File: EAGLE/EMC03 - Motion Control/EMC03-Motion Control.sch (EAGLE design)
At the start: 206 parts, among them J1 UART0, J10 67997-108HLF, J11 67997-108HLF, J12 67997-108HLF, J13 67997-108HLF, J14 67997-108HLF, J15 67997-108HLF, J2 SWD, J3 USB-B, J4 MicroSD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

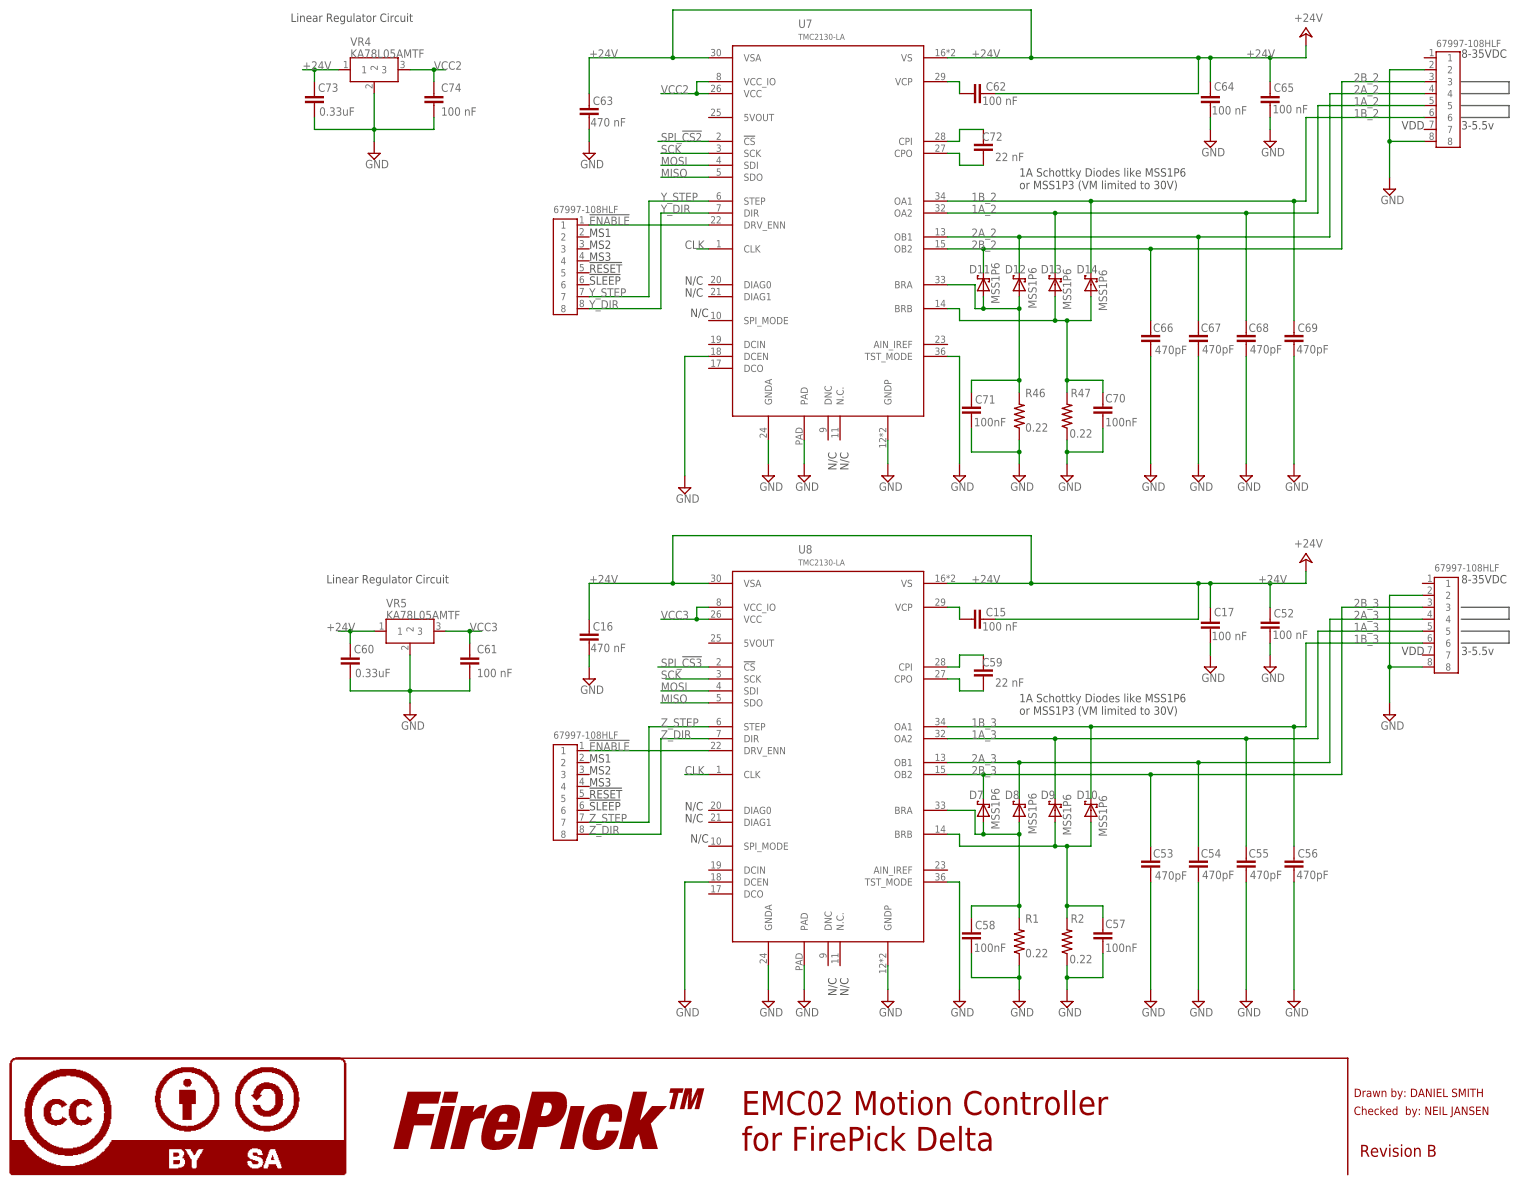
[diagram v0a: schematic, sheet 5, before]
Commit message: Updated BOM, Database, Schematic for final parts
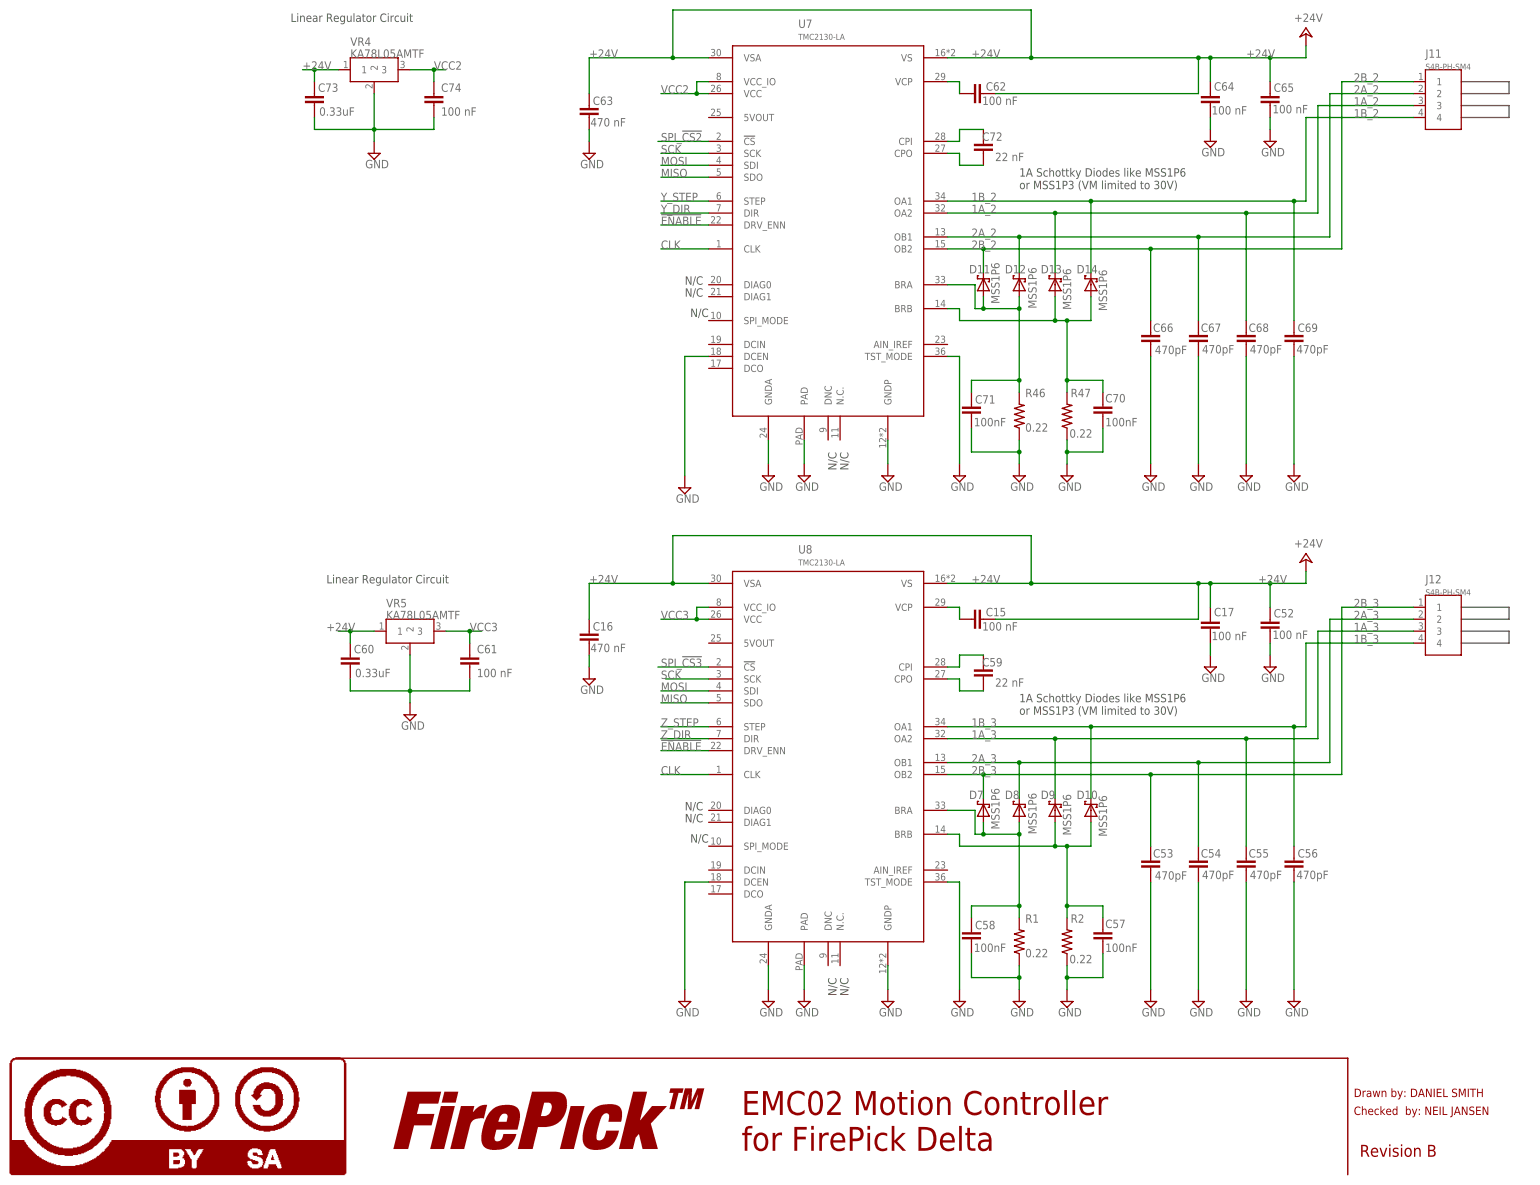
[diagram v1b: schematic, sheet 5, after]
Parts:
- removed J13, J14, J15: 67997-108HLF, TinWhiskers:CPL-CON-HEADER-0.1IN-8P-M
- J10, J11, J12: value 67997-108HLF -> S4B-PH-SM4; device TinWhiskers:CPL-CON-HEADER-0.1IN-8P-M -> TinWhiskers:CPL-CON-JST-2.0MM-4P-M-RA; PARTNO 67997-108HLF -> (none)
- J5, J6: value 68000-103HLF -> S3B-PH-SM4; device TinWhiskers:CPL-CON-HEADER-0.1IN-3P-M -> TinWhiskers:CPL-CON-JST-2.0MM-3P-M-RA; PARTNO 68000-103HLF -> S3B-PH-SM4-TB(LF)(SN)
- J7: value 68000-103HLF -> S3B-PH-SM4; device TinWhiskers:CPL-CON-HEADER-0.1IN-3P-M -> TinWhiskers:CPL-CON-JST-2.0MM-3P-M-RA; PARTNO 68000-103HLF -> S3B-PH-SM4-TB(LG)(SN)
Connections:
- removed net !RESET!: J10.5
- removed net !SLEEP!: J10.6
- removed net MS1: J10.2
- removed net MS2: J10.3
- removed net MS3: J10.4
- removed net VBAT: U1.VBAT
- net !ENABLE: no longer J10.1, J12.1, J14.1
- net +3V3: now also U1.VBAT
- net 1A_1: now also J10.3; no longer J11.5
- net 1A_2: now also J11.3; no longer J13.5
- net 1A_3: now also J12.3; no longer J15.5
- net 1B_1: now also J10.4; no longer J11.6
- net 1B_2: now also J11.4; no longer J13.6
- net 1B_3: now also J12.4; no longer J15.6
- net 2A_1: now also J10.2; no longer J11.4
- net 2A_2: now also J11.2; no longer J13.4
- net 2A_3: now also J12.2; no longer J15.4
- net 2B_1: now also J10.1; no longer J11.3
- net 2B_2: now also J11.1; no longer J13.3
- net 2B_3: now also J12.1; no longer J15.3
- net GND: no longer J11.2, J11.8, J13.2, J13.8, J15.2, J15.8
- net X_DIR: no longer J10.8
- net X_STEP: no longer J10.7
- net Y_DIR: no longer J12.8
- net Y_STEP: no longer J12.7
- net Z_DIR: no longer J14.8
- net Z_STEP: no longer J14.7
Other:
- note removed: "!RESET"
- note removed: "!SLEEP"
- note removed: "3-5.5v"
- note removed: "8-35VDC"
- note removed: "MS1"
- note removed: "MS2"
- note removed: "MS3"

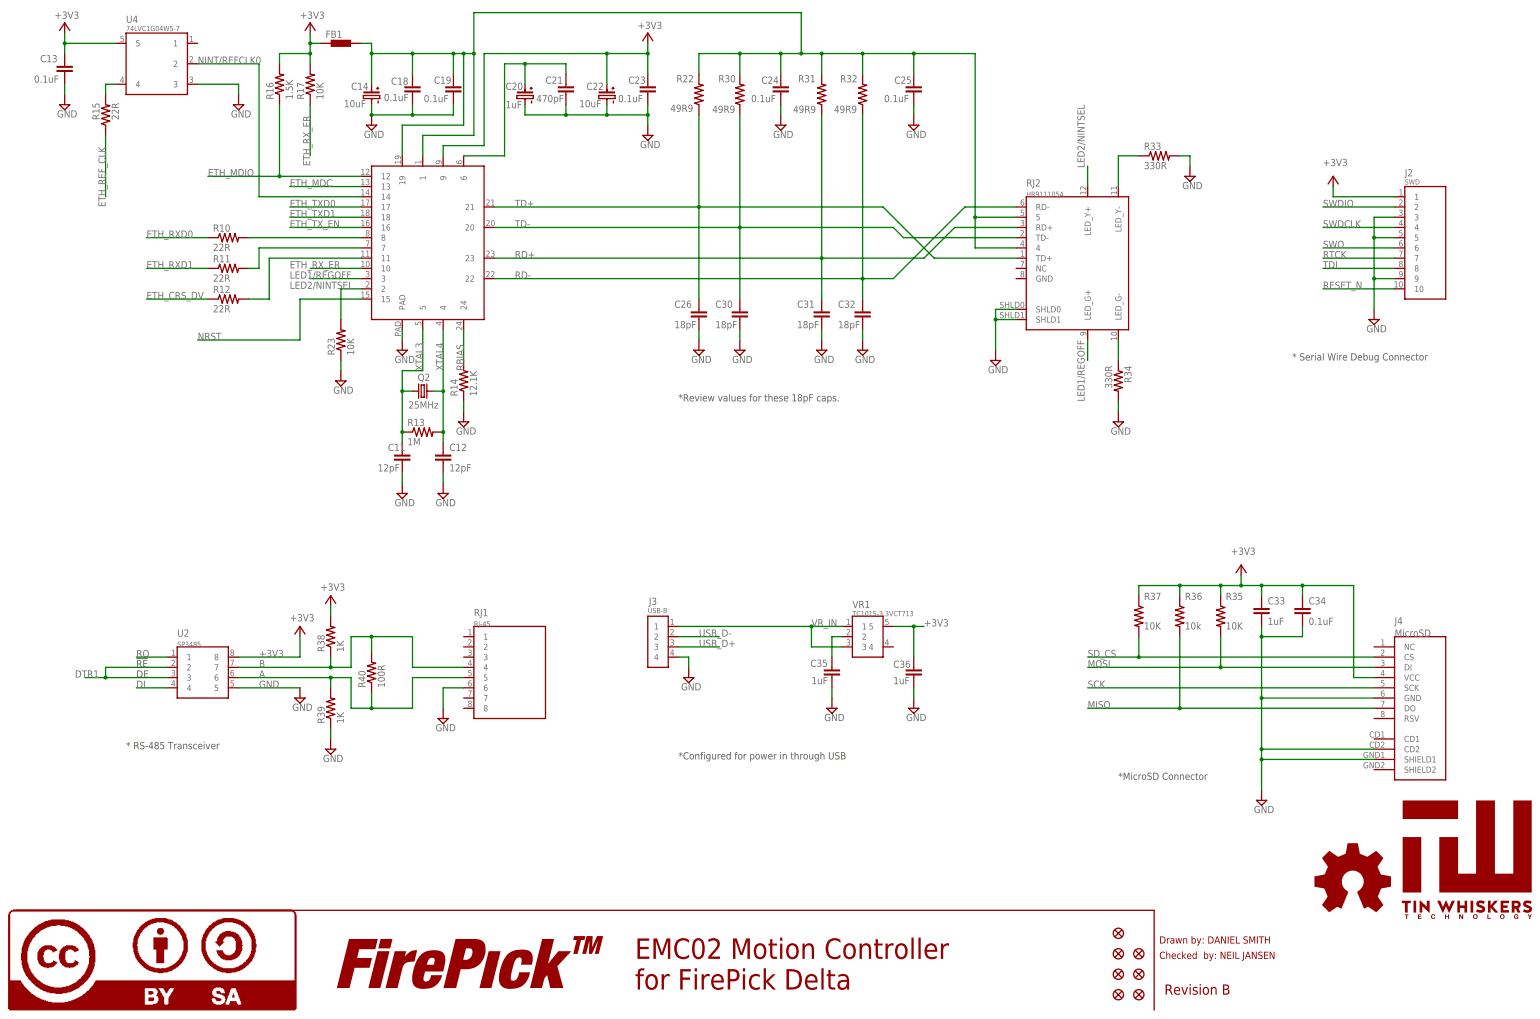
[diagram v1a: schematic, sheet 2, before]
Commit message: EMC03: Updated schematic, BOM, database, and parts library to include all revisions. This includes schematic capture for interfaces (endstops, motors, encoders, RS-485 interface, modular tools 1 and 2, the up-looking camera, the end effector the SWD connector, and the power jack).
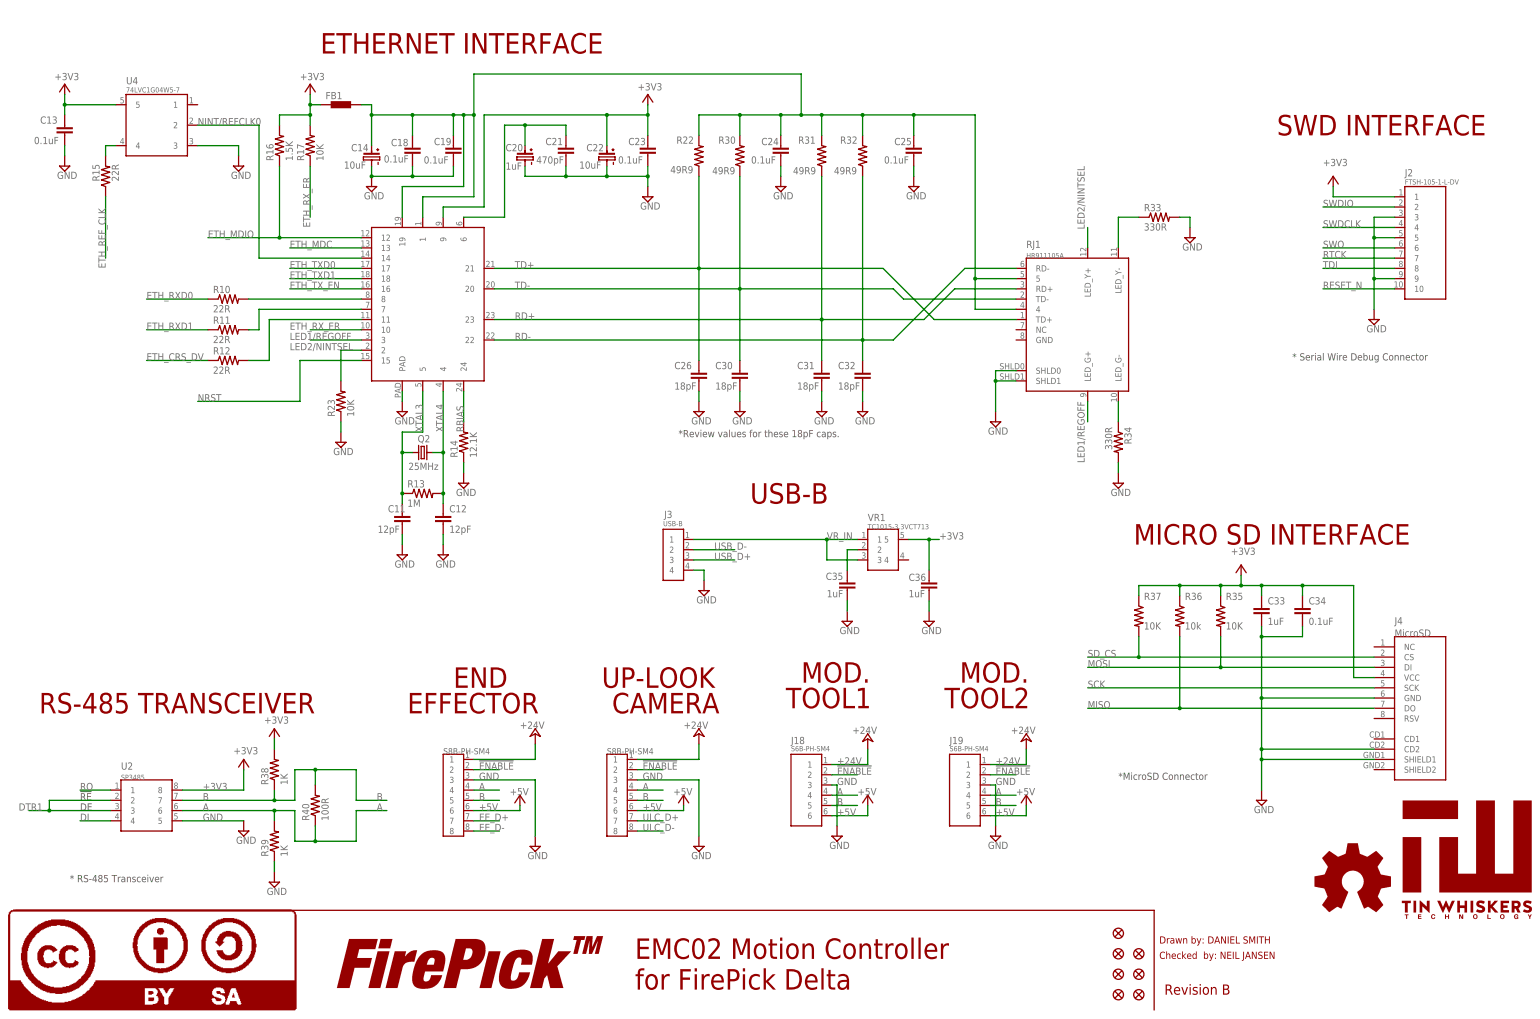
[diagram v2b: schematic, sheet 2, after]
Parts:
- removed RJ2: HR911105A, TinWhiskers:CPL-ETH-MACJACK-LED-SHLD
- added J13, J14, J15: S5B-PH-SM4, TinWhiskers:CPL-CON-JST-2.0MM-5P-M-RA
- added J16, J17: S8B-PH-SM4, TinWhiskers:CPL-CON-JST-2.0MM-8P-M-RA
- added J18, J19: S6B-PH-SM4, TinWhiskers:CPL-CON-JST-2.0MM-6P-M-RA
- C76: PARTNO (none) -> LMK107B7474KA-T
- J10, J11, J12: PARTNO (none) -> S4B-PH-SM4-TB(LF)(SN)
- J2: value SWD -> FTSH-105-1-L-DV; PARTNO TBD -> FTSH-105-01-L-DV
- J7: PARTNO S3B-PH-SM4-TB(LG)(SN) -> S3B-PH-SM4-TB(LF)(SN)
- J8: value TBD -> 694106106102; device TinWhiskers:CPL-CON-HEADER-0.1IN-6P-M -> TinWhiskers:CPL-CON-BARREL-2.1MM-24V; PARTNO * -> 694106106102
- Q1: PARTNO HCM49-12.000 -> HCM4912000000ABJT
- Q2: PARTNO HCM49-25.000MABJ -> HCM4925000000MABJ
- RJ1: value RJ-45 -> HR911105A; device TinWhiskers:CPL-CON-MOD-RJ45 -> TinWhiskers:CPL-ETH-MACJACK-LED-SHLD; PARTNO 1-5406721-3 -> HR911105A
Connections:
- new net EE_D+: J16.7
- new net EE_D-: J16.8
- new net ENCX_A: J13.2
- new net ENCX_B: J13.3
- new net ENCY_B: J14.3
- new net ENCZ_A: J15.2
- new net ENCZ_B: J15.3
- new net ENXY_A: J14.2
- new net ULC_D+: J17.7
- new net ULC_D-: J17.8
- new net X_INDEX: J13.4
- new net Y_INDEX: J14.4
- new net Z_INDEX: J15.4
- net !ENABLE: now also J16.2, J17.2, J18.2, J19.2
- net +24V: now also J16.1, J17.1, J18.1, J19.1, J8.2; no longer J8.1
- net +5V: now also J13.1, J14.1, J15.1, J16.6, J17.6, J18.6, J19.6
- net A: now also J16.4, J17.4, J18.4, J19.4; no longer RJ1.5
- net B: now also J16.5, J17.5, J18.5, J19.5; no longer RJ1.4
- net GND: now also J13.5, J14.5, J15.5, J16.3, J17.3, J18.3, J19.3, RJ1.SHLD0, RJ1.SHLD1; no longer RJ1.6, RJ2.SHLD0, RJ2.SHLD1
- net LED1/REGOFF: now also RJ1.LED_G+; no longer RJ2.LED_G+
- net LED2/NINTSEL: now also RJ1.LED_Y+; no longer RJ2.LED_Y+
- net N$6: now also RJ1.4, RJ1.5; no longer RJ2.4, RJ2.5
- net N$7: now also RJ1.LED_Y-; no longer RJ2.LED_Y-
- net N$8: now also RJ1.LED_G-; no longer RJ2.LED_G-
- net RD+: now also RJ1.RD+; no longer RJ2.RD+
- net RD-: now also RJ1.RD-; no longer RJ2.RD-
- net TD+: now also RJ1.TD+; no longer RJ2.TD+
- net TD-: now also RJ1.TD-; no longer RJ2.TD-
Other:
- note added: "CAMERA"
- note added: "EFFECTOR"
- note added: "END"
- note added: "ETHERNET INTERFACE"
- note added: "MICRO SD INTERFACE"
- note added: "MOD."
- note added: "OPTICAL ENCODERS"
- note added: "RS-485 TRANSCEIVER"
- note added: "SWD INTERFACE"
- note added: "TOOL1"
- note added: "TOOL2"
- note added: "UP-LOOK"
- note added: "USB-B"
- note removed: "* NOTE: THIS IS A 2-PIECE TERMINAL STRIP. - THE OSTOP IS THE MALE PIN HEADER - THE OSTTH IS THE PLUG-ON SCREW TERMINAL"
- note removed: "*Configured for power in through USB"
- moved on the sheet: C11, C12, C13, C14, C18, C19, C2, C20, C21, C22, C23, C24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

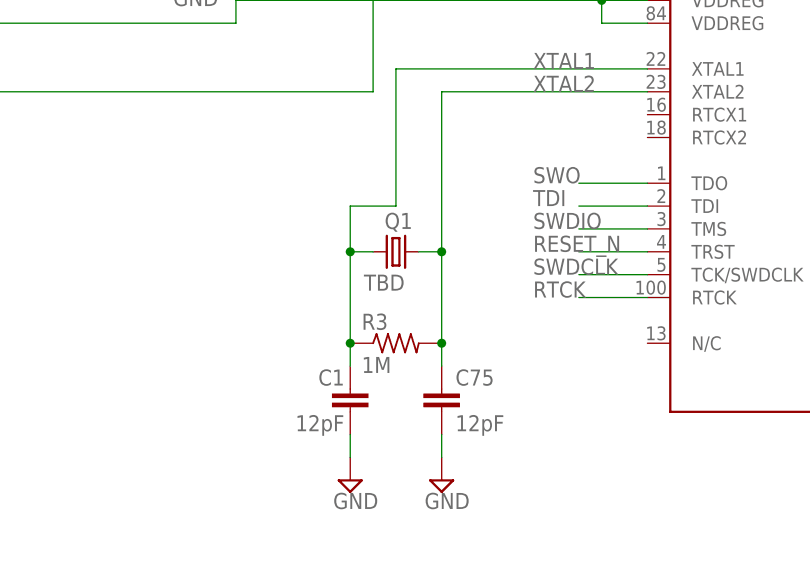
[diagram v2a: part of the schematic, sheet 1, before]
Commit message: Resized EMC03 board, 50mm per side. All connector 3D models have been imported for design in Cubify. Database has been updated to include E-stop connector (corrected). Connectors have been added to board. The board is not large enough for all edge connectors to fit.
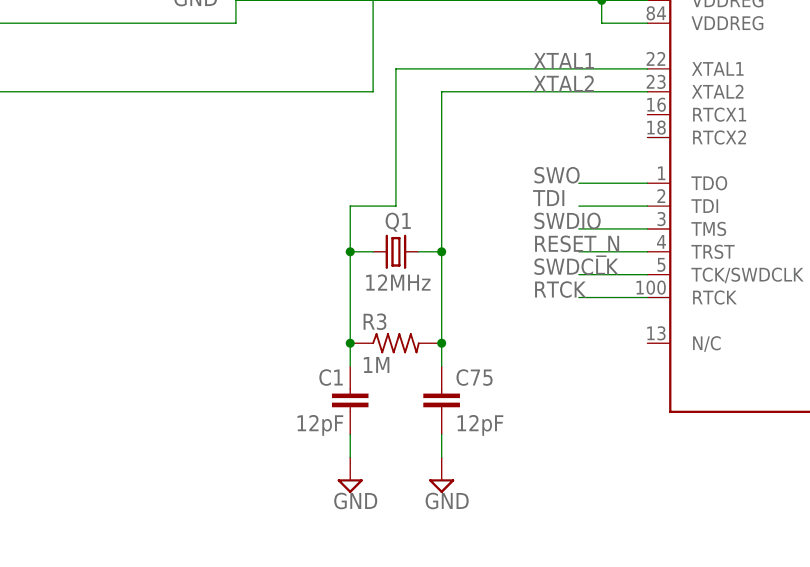
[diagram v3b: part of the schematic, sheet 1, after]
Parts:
- J9: value 68000-102HLF -> S2B-PH-SM4; PARTNO 68000-102HLF -> S2B-PH-SM4-TB(LF)(SN)
- Q1: value TBD -> 12MHz
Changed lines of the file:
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@@
 <setting verticaltext="up"/>
 </settings>
-<grid distance="0.05" unitdist="inch" unit="inch" style="lines" multiple="1" display="yes" altdistance="0.025" altunitdist="inch" altunit="inch"/>
+<grid distance="0.1" unitdist="inch" unit="inch" style="lines" multiple="1" display="no" altdistance="0.01" altunitdist="inch" altunit="inch"/>
 <layers>
 <layer number="1" name="Top" color="4" fill="1" visible="no" active="no"/>
@@
 <part name="P+7" library="supply1" deviceset="+3V3" device=""/>
 <part name="GND36" library="TinWhiskers" deviceset="GND" device=""/>
-<part name="J9" library="TinWhiskers" deviceset="CPL-CON-HEADER-0.1IN-2P-M" device="" value="68000-102HLF">
-<attribute name="PARTNO" value="68000-102HLF"/>
+<part name="J9" library="TinWhiskers" deviceset="CPL-CON-HEADER-0.1IN-2P-M" device="" value="S2B-PH-SM4">
+<attribute name="PARTNO" value="S2B-PH-SM4-TB(LF)(SN)"/>
 </part>
 <part name="R29" library="TinWhiskers" deviceset="CPL-RES-0603-4.7K-0.1W" device="" value="4.7K">
@@
 <part name="+3V15" library="supply1" deviceset="+3V3" device=""/>
 <part name="+3V16" library="supply1" deviceset="+3V3" device=""/>
-<part name="Q1" library="TinWhiskers" deviceset="CPL-OSC-CRY-12MHZ-18PF" device="" value="TBD">
+<part name="Q1" library="TinWhiskers" deviceset="CPL-OSC-CRY-12MHZ-18PF" device="" value="12MHz">
 <attribute name="PARTNO" value="HCM4912000000ABJT"/>
 </part>
